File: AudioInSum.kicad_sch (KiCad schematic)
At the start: 14 parts

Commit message: Fixed ultralibrarian library with capital letter difference
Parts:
- U9: footprint UltraLibrarian:D8_TEX -> Ultralibrarian:D8_TEX
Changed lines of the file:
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@@
       (effects (font (size 1.27 1.27)))
     )
-    (property "Footprint" "UltraLibrarian:D8_TEX" (at 154.94 56.515 0)
+    (property "Footprint" "Ultralibrarian:D8_TEX" (at 154.94 56.515 0)
       (effects (font (size 1.27 1.27)) hide)
     )
@@
       (effects (font (size 1.27 1.27)))
     )
-    (property "Footprint" "UltraLibrarian:D8_TEX" (at 140.97 143.51 0)
+    (property "Footprint" "Ultralibrarian:D8_TEX" (at 140.97 143.51 0)
       (effects (font (size 1.27 1.27)) hide)
     )
@@
       (effects (font (size 1.27 1.27)))
     )
-    (property "Footprint" "UltraLibrarian:D8_TEX" (at 154.305 105.41 0)
-      (effects (font (size 1.27 1.27)) hide)
-    )
+    (property "Footprint" "Ultralibrarian:D8_TEX" (at 154.305 105.41 0)
+      (effects (font (size 1.27 1.27)) hide)
+    )

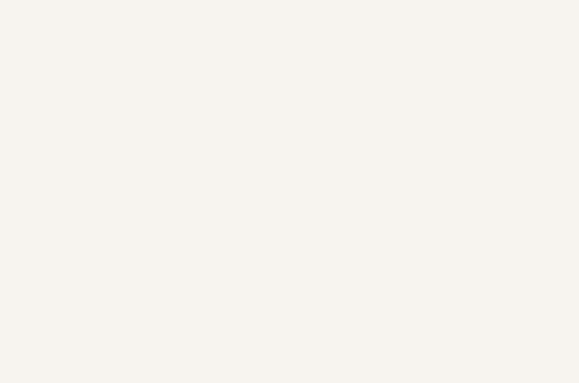
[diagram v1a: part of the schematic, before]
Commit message: adding mono connectors, CV, and gate as well
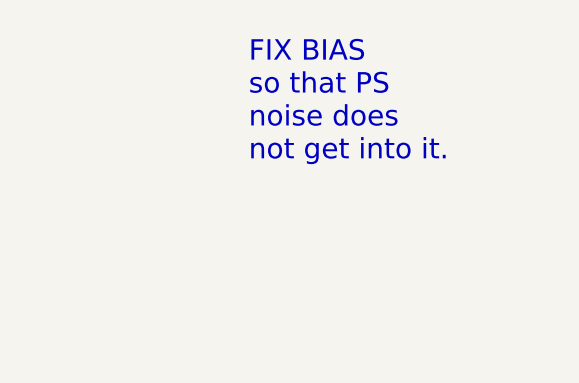
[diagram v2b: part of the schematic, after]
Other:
- note added: "FIX BIAS so that PS noise does not get into it."
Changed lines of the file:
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@@
+    (effects (font (size 2.27 2.27)) (justify left bottom))
+  )
+  (text "FIX BIAS\nso that PS\nnoise does\nnot get into it." (at 243.332 32.512 0)
     (effects (font (size 2.27 2.27)) (justify left bottom))
   )

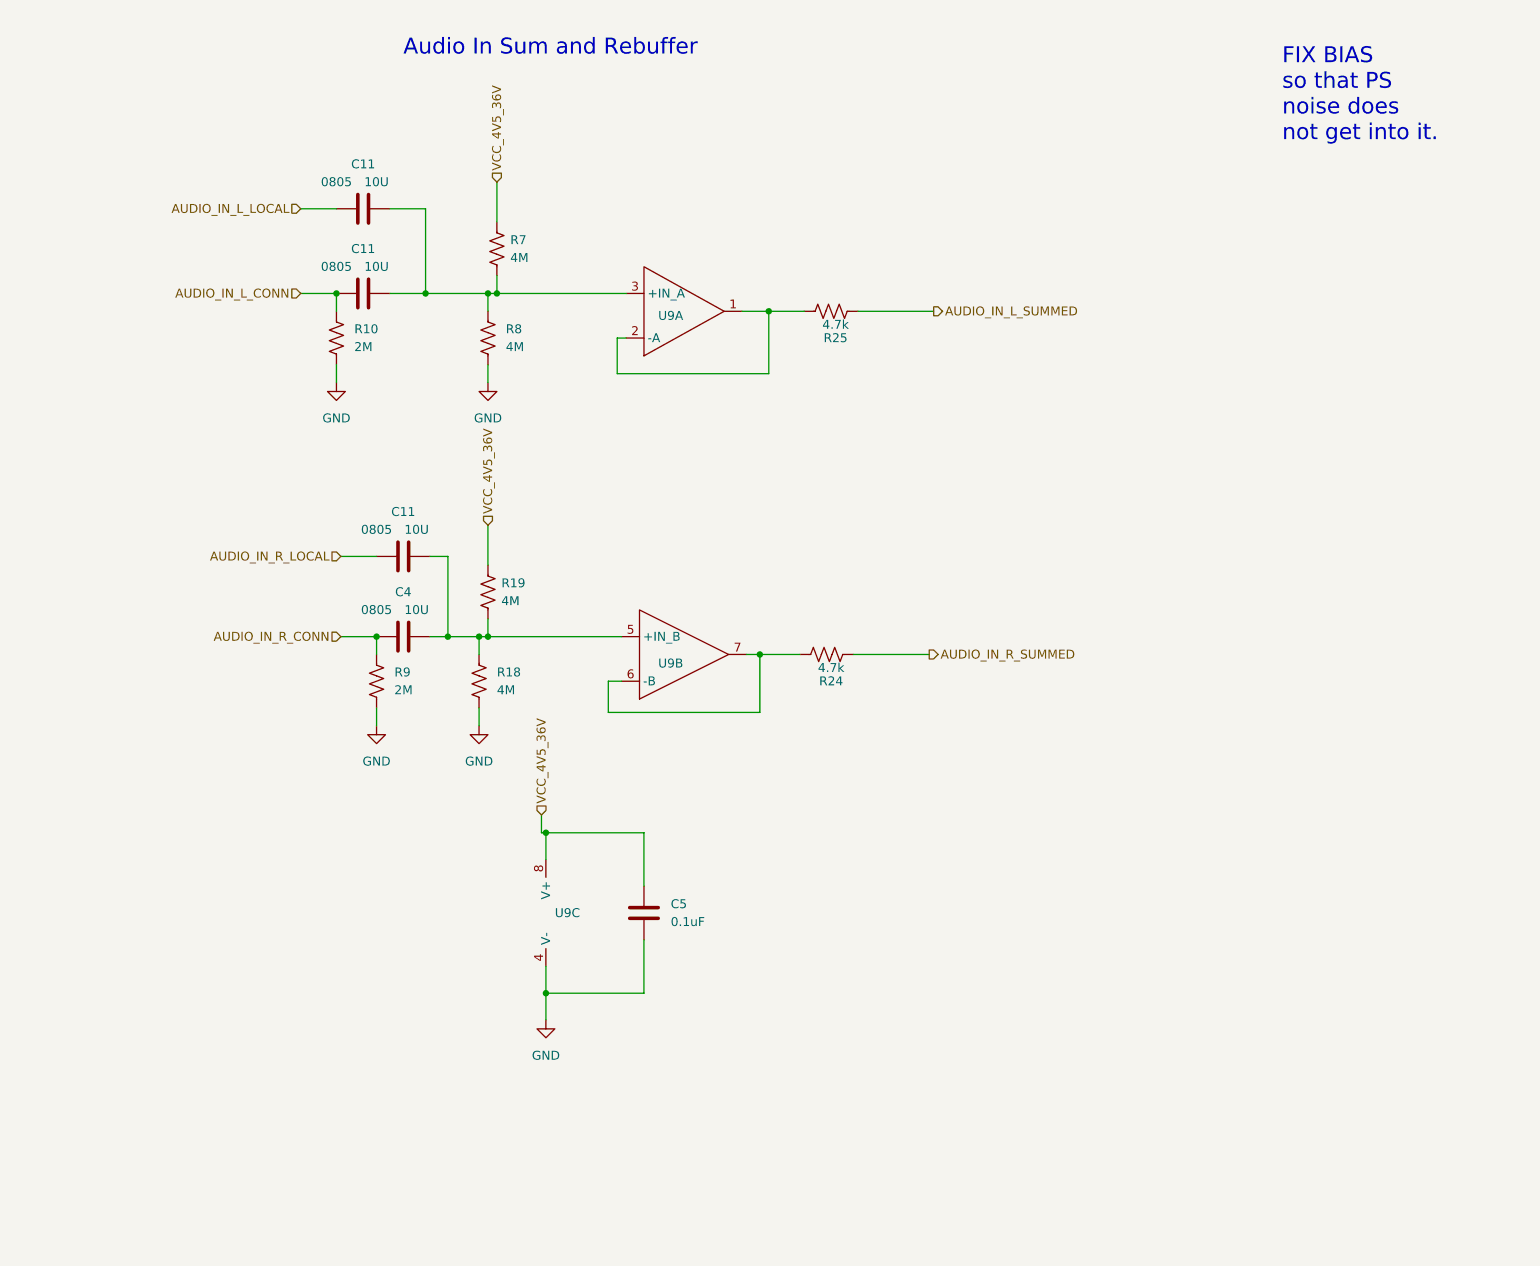
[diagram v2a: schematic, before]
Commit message: Add USB 5V switcher, adjust audio in circuit
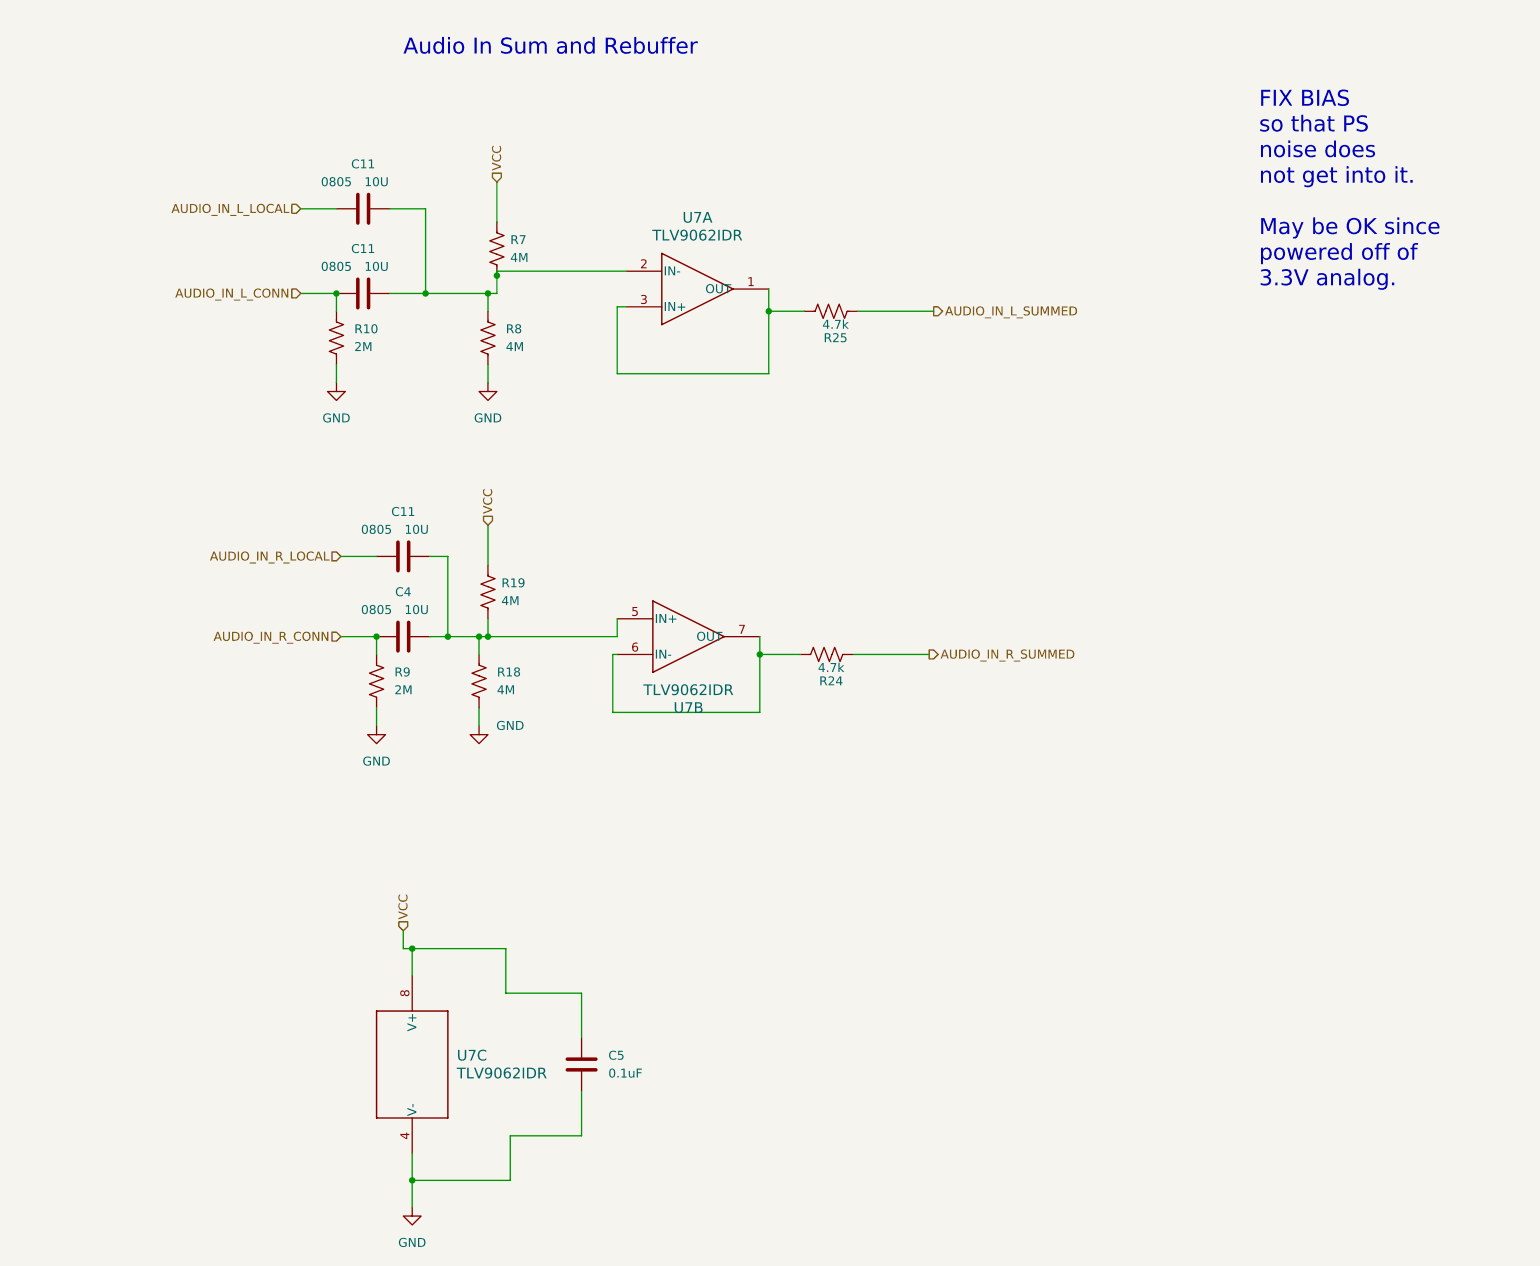
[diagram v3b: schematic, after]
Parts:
- removed U9: ~, Ultralibrarian:D8_TEX, symbol Ultralibrarian_modified_symbols:OPA1688_SOIC8
- added U7: TLV9062IDR, D0008A_N, symbol 2023-10-05_02-35-21:TLV9062IDR
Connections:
- net GND: now also U7.4 (V-)
- net at R24.2: now also U7.6 (IN-), U7.7 (OUT)
- net at R25.2: now also U7.1 (OUT), U7.3 (IN+)
- net at C11.2, C11.2, R7.2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: now also U7.2 (IN-)
- net at C11.2, C4.2, R18.1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: now also U7.5 (IN+)
- net VCC_4V5_36V renamed VCC
- net VCC: now also U7.8 (V+)
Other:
- note added: "FIX BIAS so that PS noise does not get into it. May be OK since powered off of 3.3V analog."
- note removed: "FIX BIAS so that PS noise does not get into it."
- moved on the sheet: C5

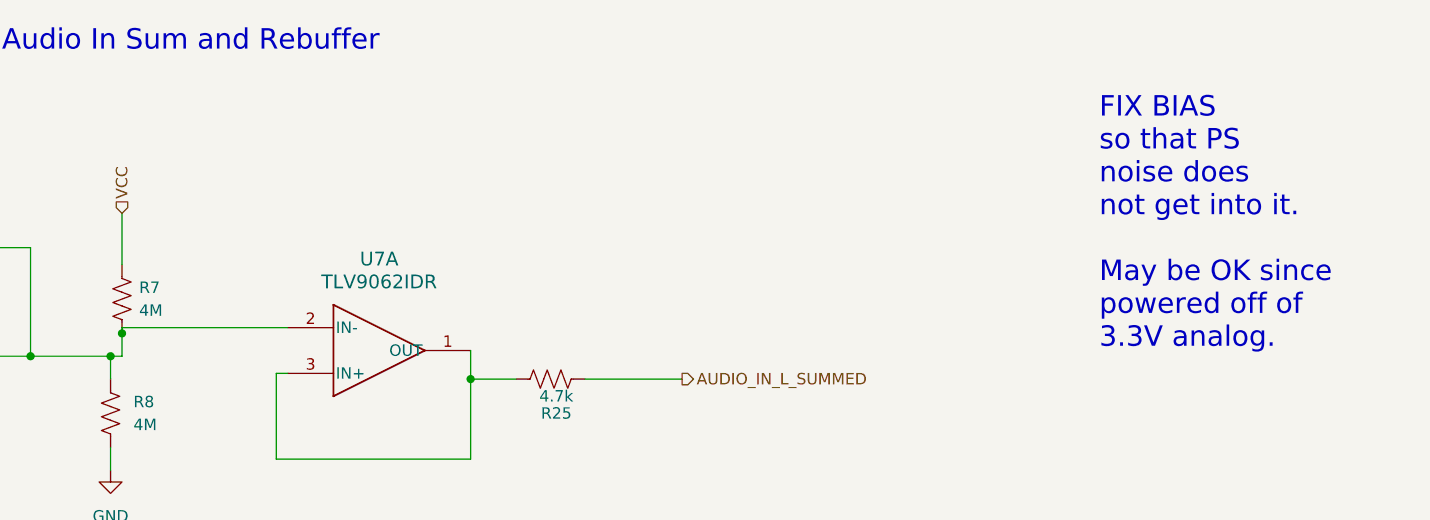
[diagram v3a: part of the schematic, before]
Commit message: Update Audio out to switch between 1V ptp or 10V ptp based on jumper
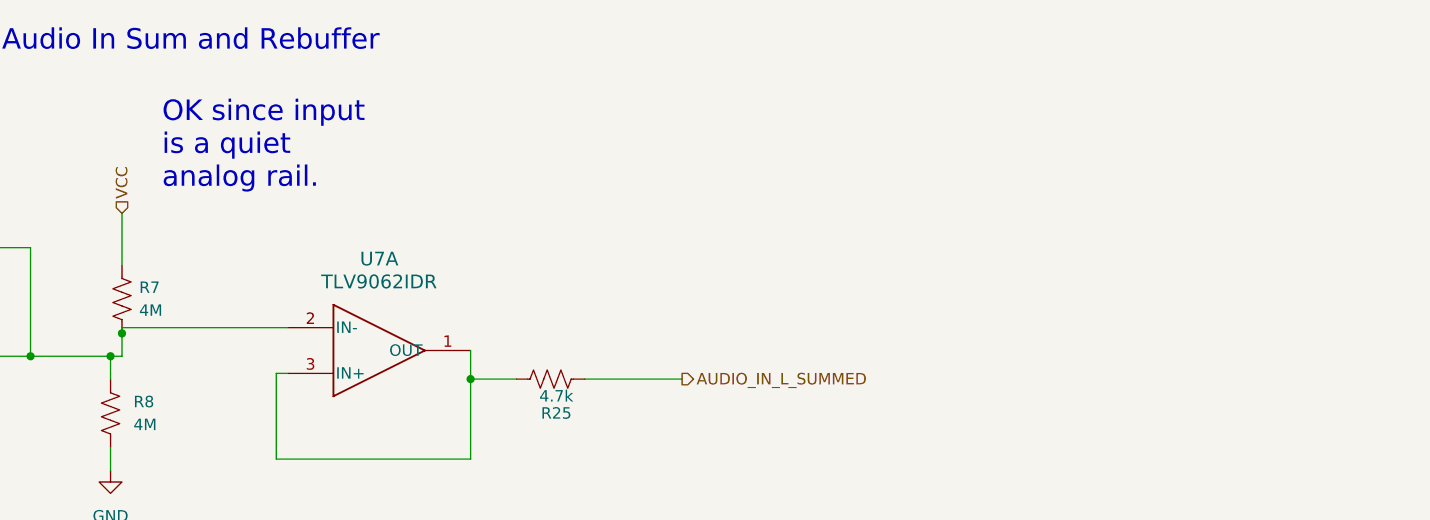
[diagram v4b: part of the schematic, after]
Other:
- note added: "OK since input is a quiet analog rail."
- note removed: "FIX BIAS so that PS noise does not get into it. May be OK since powered off of 3.3V analog."
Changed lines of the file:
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@@
     (effects (font (size 2.27 2.27)) (justify left bottom))
   )
-  (text "FIX BIAS\nso that PS\nnoise does\nnot get into it.\n\nMay be OK since\npowered off of\n3.3V analog."
-    (at 240.03 53.34 0)
+  (text "OK since input\nis a quiet\nanalog rail." (at 135.89 35.56 0)
     (effects (font (size 2.27 2.27)) (justify left bottom))
   )

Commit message: getting closer
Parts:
- added R25 (x2): 0, Resistor_SMD:R_0402_1005Metric, symbol Device:R_US
- added R25 (x2): DNP, Resistor_SMD:R_0402_1005Metric, symbol Device:R_US
- R18, R19, R7, R8: value 4M -> 2M
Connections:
- net GND: now also R25.2, R25.2
- net at R24.2, U7.7 (OUT): now also R25.1; no longer U7.6 (IN-)
- net at R25.2, U7.1 (OUT): now also R25.1; no longer U7.3 (IN+)
- net at C11.2, C11.2, R7.2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: now also U7.3 (IN+); no longer U7.2 (IN-)
- new net: R25.1, R25.2, U7.2 (IN-)
- new net: R25.1, R25.2, U7.6 (IN-)
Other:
- moved on the sheet: R24, U7B
